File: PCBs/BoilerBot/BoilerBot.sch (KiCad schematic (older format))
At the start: 24 parts

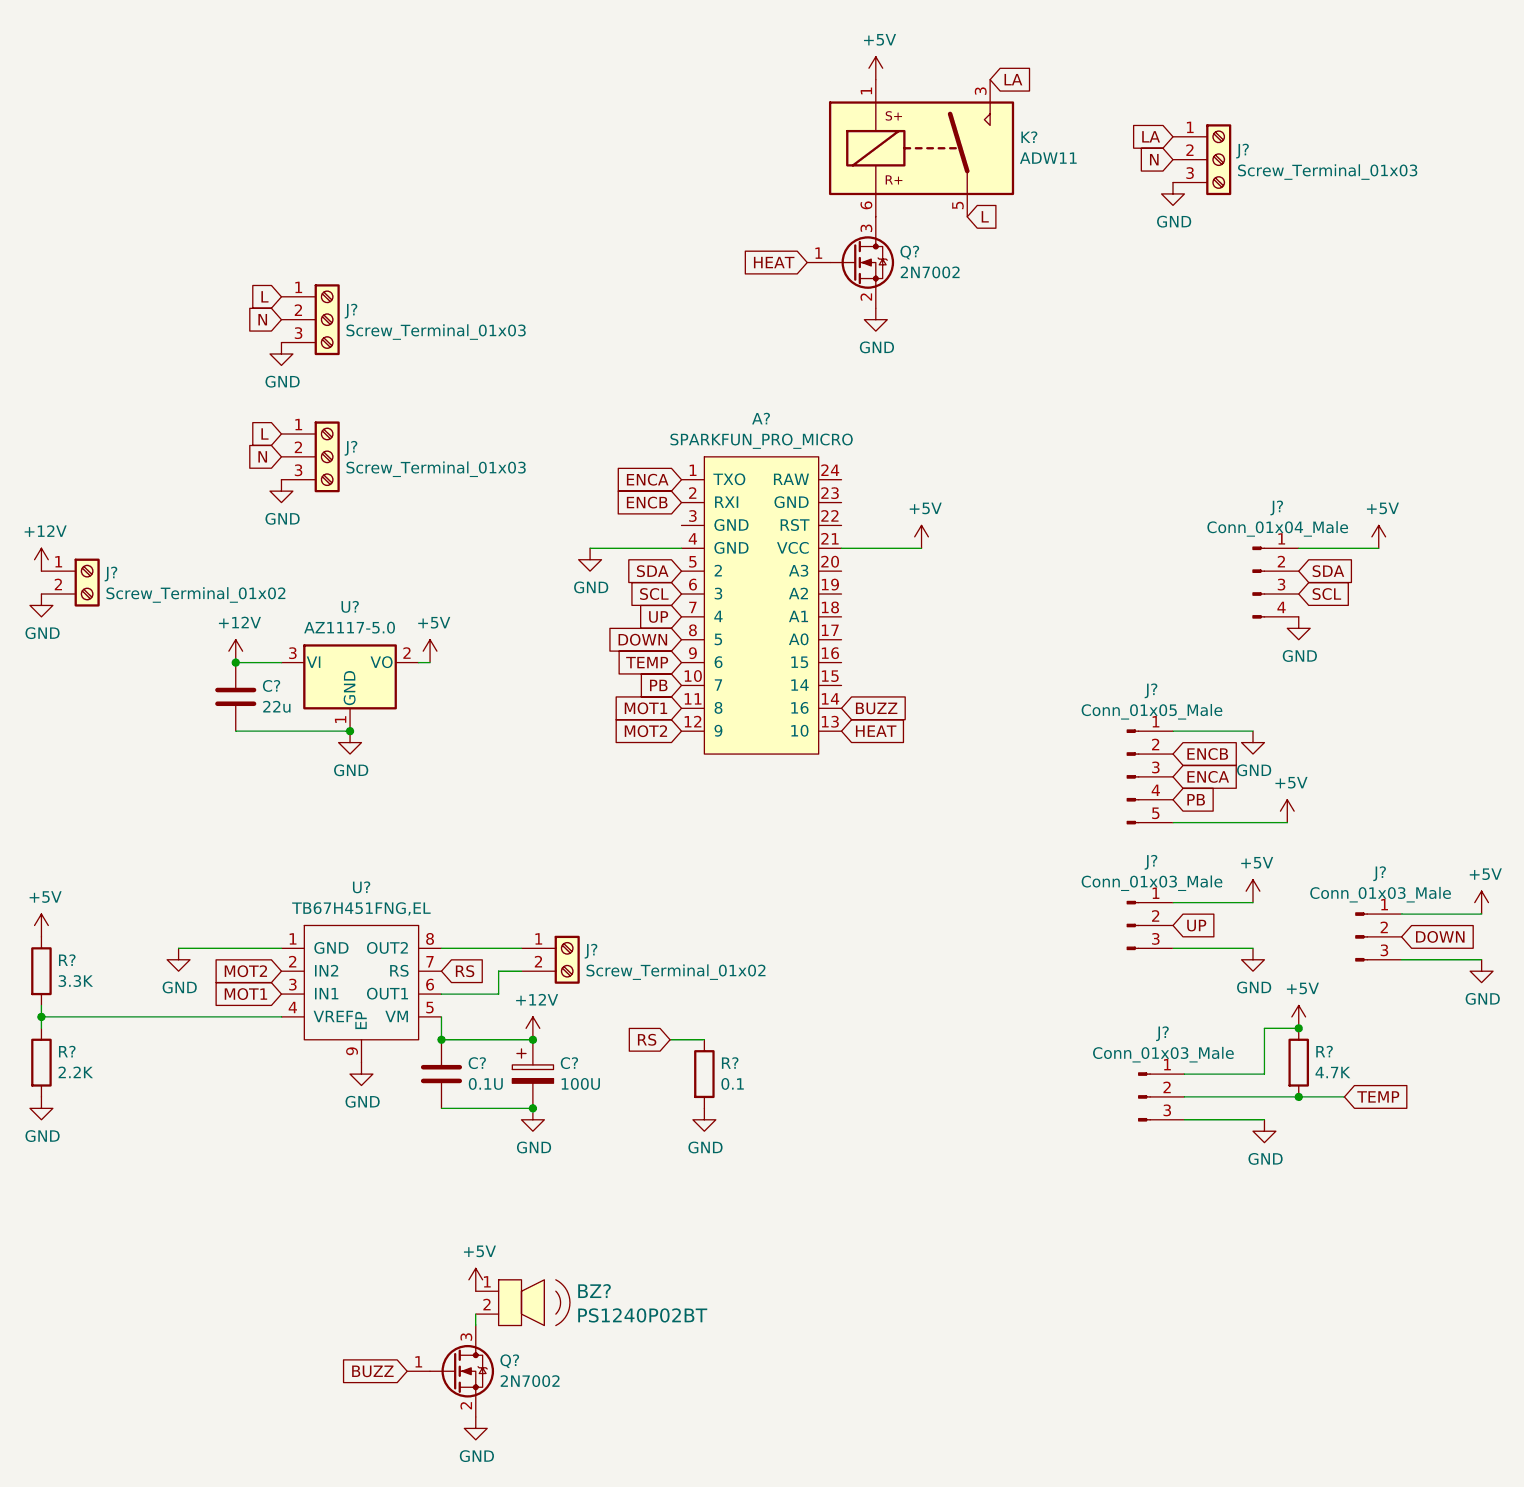
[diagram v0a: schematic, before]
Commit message: started pcb layout
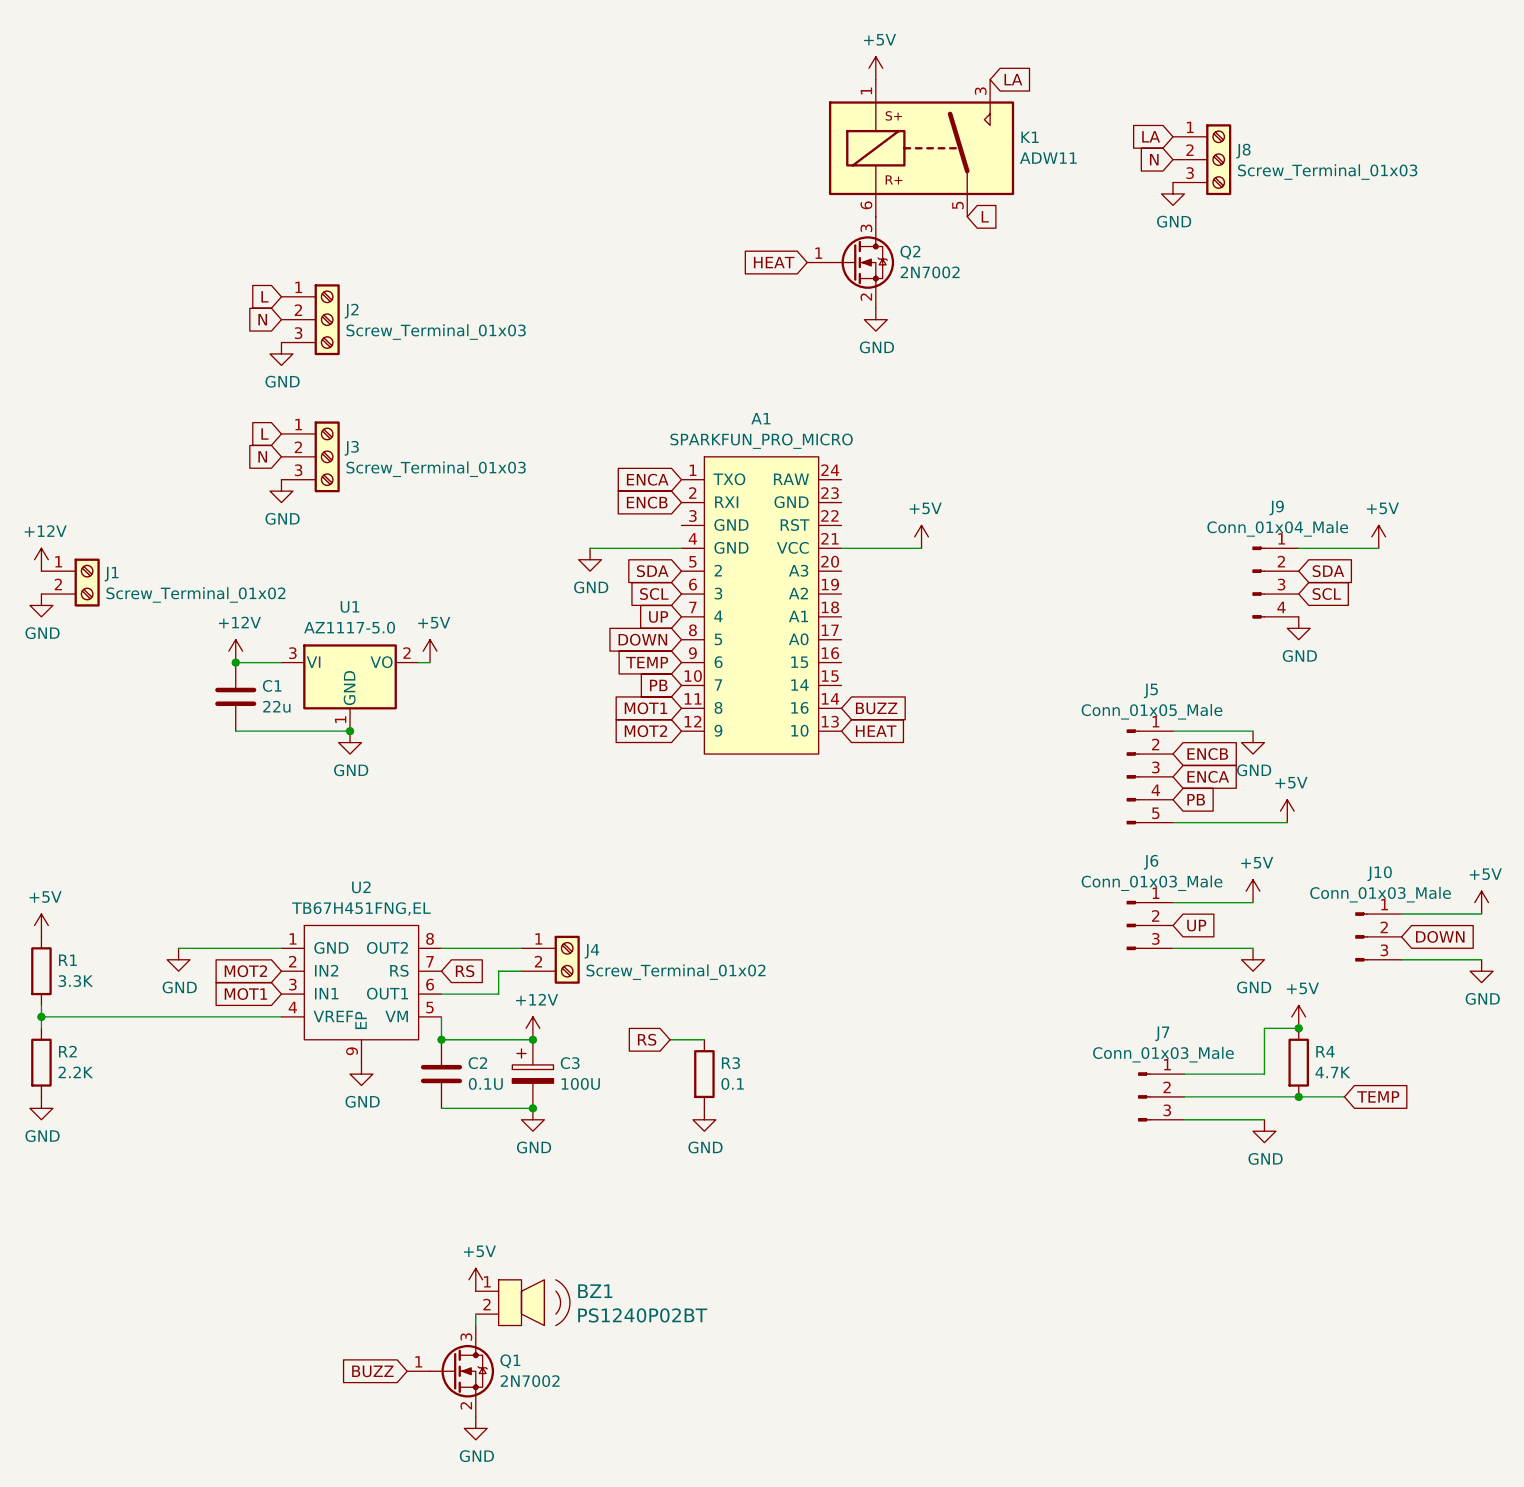
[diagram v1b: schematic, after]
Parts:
- A1: renamed from A?; footprint (none) -> BoilerBot:SPARKFUN_PRO_MICRO
- BZ1: renamed from BZ?; footprint digikey-footprints:Piezo_Transducer_THT_PS1240P02BT -> BoilerBot:PUI_AT-1224-TWT-5V-2-R
- C1, C2, C3: renamed from C?; footprint (none) -> Capacitor_SMD:C_0805_2012Metric_Pad1.18x1.45mm_HandSolder
- J1, J4: renamed from J?; footprint (none) -> TerminalBlock_Phoenix:TerminalBlock_Phoenix_PT-1,5-2-5.0-H_1x02_P5.00mm_Horizontal
- J10, J6, J7: renamed from J?; footprint (none) -> Connector_JST:JST_XH_B3B-XH-A_1x03_P2.50mm_Vertical
- J2, J3, J8: renamed from J?; footprint (none) -> TerminalBlock_Phoenix:TerminalBlock_Phoenix_PT-1,5-3-5.0-H_1x03_P5.00mm_Horizontal
- J5: renamed from J?; footprint (none) -> Connector_JST:JST_PH_B5B-PH-K_1x05_P2.00mm_Vertical
- J9: renamed from J?; footprint (none) -> Connector_JST:JST_XH_B4B-XH-A_1x04_P2.50mm_Vertical
- R1, R2, R3, R4: renamed from R?; footprint (none) -> Resistor_SMD:R_0805_2012Metric_Pad1.20x1.40mm_HandSolder
- U1: renamed from U?; footprint (none) -> Package_TO_SOT_SMD:SOT-223-3_TabPin2
- U2: renamed from U?; footprint (none) -> Package_SO:SOIC-8-1EP_3.9x4.9mm_P1.27mm_EP2.29x3mm_ThermalVias
- gave numbers to parts that had none: 3

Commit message: PCBs ready to order
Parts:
- C3: footprint Capacitor_SMD:C_0805_2012Metric_Pad1.18x1.45mm_HandSolder -> Capacitor_SMD:CP_Elec_6.3x7.7
- K1: footprint Relay_THT:Relay_1P1T_NO_10x24x18.8mm_Panasonic_ADW11xxxxW_THT -> BoilerBot:OMRON_G5PZ-1A
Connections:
- net DOWN: now also A1.11 (8); no longer A1.8 (5)
- net MOT1: now also A1.7 (4); no longer A1.11 (8)
- net MOT2: now also A1.8 (5); no longer A1.12 (9)
- net TEMP: now also A1.12 (9); no longer A1.9 (6)
- net UP: now also A1.9 (6); no longer A1.7 (4)
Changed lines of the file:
@@
 Text GLabel 5200 3800 0    50   Input ~ 0
 SCL
+Text GLabel 5200 4100 0    50   Input ~ 0
+UP
+Text GLabel 5200 4300 0    50   Input ~ 0
+DOWN
 Text GLabel 5200 3900 0    50   Input ~ 0
-UP
+MOT1
 Text GLabel 5200 4000 0    50   Input ~ 0
-DOWN
-Text GLabel 5200 4300 0    50   Input ~ 0
-MOT1
+MOT2
 Text GLabel 5200 4400 0    50   Input ~ 0
-MOT2
-Text GLabel 5200 4100 0    50   Input ~ 0
 TEMP
 Text GLabel 5900 4400 2    50   Input ~ 0
@@
 F 0 "C3" H 4668 5946 50  0000 L CNN
 F 1 "100U" H 4668 5855 50  0000 L CNN
-F 2 "Capacitor_SMD:C_0805_2012Metric_Pad1.18x1.45mm_HandSolder" H 4588 5750 50  0001 C CNN
+F 2 "Capacitor_SMD:CP_Elec_6.3x7.7" H 4588 5750 50  0001 C CNN
 F 3 "~" H 4550 5900 50  0001 C CNN
 	1    4550 5900
@@
 F 0 "K1" H 6680 1896 50  0000 L CNN
 F 1 "ADW11" H 6680 1805 50  0000 L CNN
-F 2 "Relay_THT:Relay_1P1T_NO_10x24x18.8mm_Panasonic_ADW11xxxxW_THT" H 7575 1800 50  0001 C CNN
+F 2 "BoilerBot:OMRON_G5PZ-1A" H 7575 1800 50  0001 C CNN
 F 3 "https://www.panasonic-electric-works.com/pew/es/downloads/ds_dw_hl_en.pdf" H 6250 1850 50  0001 C CNN
 	1    6250 1850
